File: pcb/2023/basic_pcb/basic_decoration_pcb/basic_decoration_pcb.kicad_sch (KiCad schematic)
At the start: 16 parts, among them J1 Conn_01x15_Socket, J2 Conn_01x15_Socket, J3 Screw_Terminal_01x03, Q1 2N2219

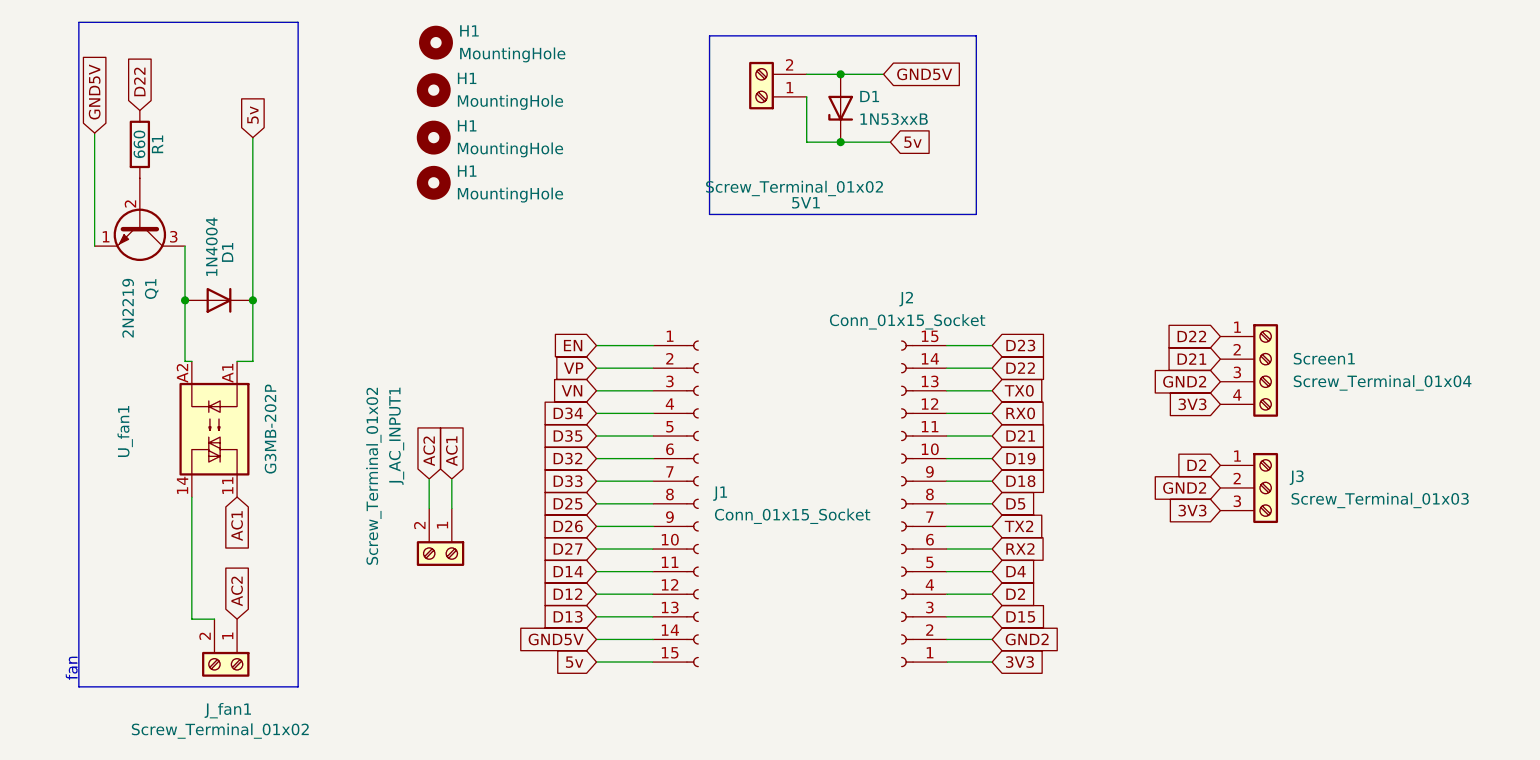
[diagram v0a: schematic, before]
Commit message: add, added custom solid state relay to the PCB by using optocouplers and triacs, also added the MOC3041 footprint to the esp32 library to keep it within our common resources
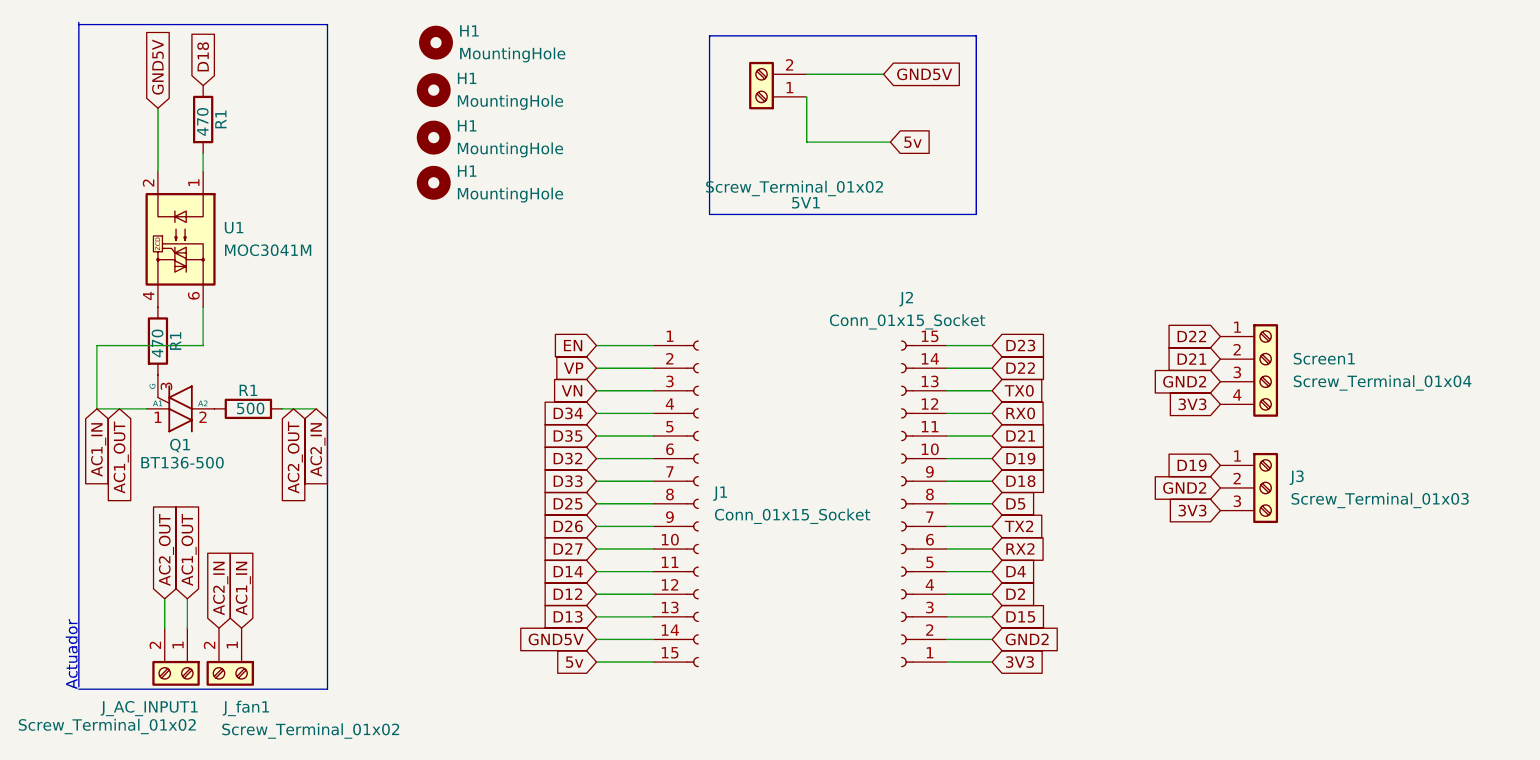
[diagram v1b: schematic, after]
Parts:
- removed D1: 1N53xxB, Diode_THT:D_DO-201_P15.24mm_Horizontal, symbol Diode:1N53xxB
- removed D1: 1N4004, Diode_THT:D_DO-41_SOD81_P10.16mm_Horizontal, symbol Diode:1N4004
- removed Q1: 2N2219, Package_TO_SOT_THT:TO-39-3, symbol Transistor_BJT:2N2219
- removed U_fan1: G3MB-202P, smart_sensor:G3MB-202P, symbol Relay_SolidState:34.81-8240
- added Q1: BT136-500, Package_TO_SOT_THT:TO-220-3_Vertical, symbol Triac_Thyristor:BT136-500
- added R1: 470, Resistor_THT:R_Axial_DIN0204_L3.6mm_D1.6mm_P5.08mm_Vertical, symbol Device:R
- added R1: 500, Resistor_THT:R_Axial_DIN0204_L3.6mm_D1.6mm_P5.08mm_Vertical, symbol Device:R
- added U1: MOC3041M, esp32:PDIP6_6P6X8P89_ONS, symbol Relay_SolidState:MOC3041M
- R1: value 660 -> 470
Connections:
- net D18: now also R1.1
- net D19: now also J3.1 (Pin_1)
- net D2: no longer J3.1 (Pin_1)
- net D22: no longer R1.1
- net GND5V: now also U1.2
- net AC2_IN: now reaches J_fan1.2 (Pin_2)
- net AC2_IN: now also J_AC_INPUT1.2 (Pin_2), R1.2
- net at R1.2: now also U1.1
- net AC1 renamed AC1_IN
- net AC1_IN: now also J_fan1.1 (Pin_1), Q1.1 (A1), U1.6
- removed net AC2: J_AC_INPUT1.2 (Pin_2), J_fan1.1 (Pin_1)
- new net: R1.1, U1.4
- new net: Q1.3 (G), R1.2
- new net: Q1.2 (A2), R1.1
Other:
- note added: "Actuador"
- note removed: "fan"
- moved on the sheet: J_fan1, R1

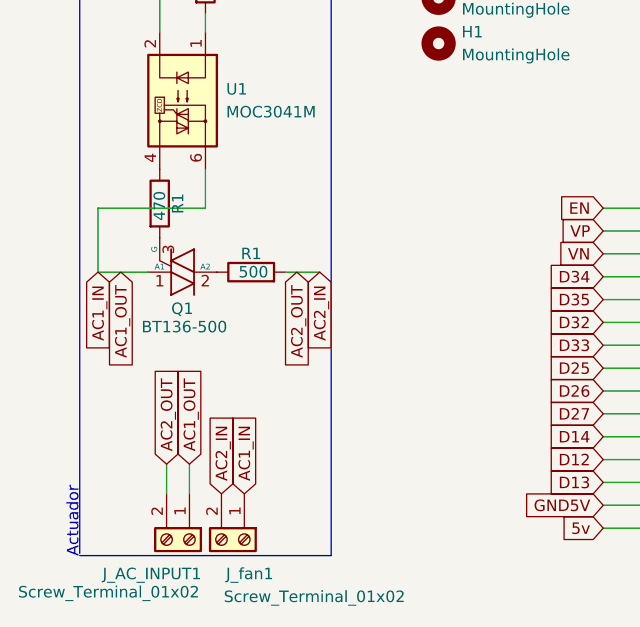
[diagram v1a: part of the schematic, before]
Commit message: update, fixed an error in the PCB and now any AC appliance which get's connected can work
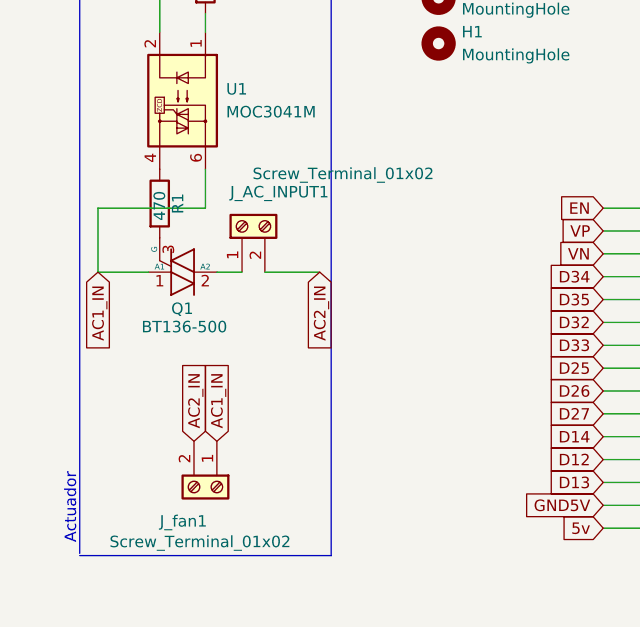
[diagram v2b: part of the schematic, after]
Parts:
- removed R1: 500, Resistor_THT:R_Axial_DIN0204_L3.6mm_D1.6mm_P5.08mm_Vertical, symbol Device:R
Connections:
- net AC1_IN: no longer J_AC_INPUT1.1 (Pin_1)
- net at Q1.2 (A2): now also J_AC_INPUT1.1 (Pin_1)
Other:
- moved on the sheet: J_fan1
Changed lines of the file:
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@@
-    (stroke (width 0) (type default))
-  )
-  (wire (pts (xy 33.528 93.98) (xy 33.528 90.678))
     (stroke (width 0) (type default))
   )
@@
     (stroke (width 0) (type default))
   )
-  (wire (pts (xy 46.736 69.342) (xy 50.546 69.342))
-    (stroke (width 0) (type default))
-  )
   (polyline (pts (xy 94.742 27.432) (xy 124.714 27.432))
     (stroke (width 0) (type default))
@@
     (stroke (width 0) (type default))
   )
+  (wire (pts (xy 39.116 69.342) (xy 41.91 69.342))
+    (stroke (width 0) (type default))
+  )
   (wire (pts (xy 105.664 39.37) (xy 115.062 39.37))
     (stroke (width 0) (type default))
@@
     (stroke (width 0) (type default))
   )
+  (wire (pts (xy 44.45 69.342) (xy 50.546 69.342))
+    (stroke (width 0) (type default))
+  )
   (wire (pts (xy 82.042 62.23) (xy 88.392 62.23))
     (stroke (width 0) (type default))
@@
     (stroke (width 0) (type default))
   )
-  (wire (pts (xy 36.068 93.98) (xy 36.068 90.678))
-    (stroke (width 0) (type default))
-  )
   (wire (pts (xy 82.042 97.79) (xy 88.392 97.79))
     (stroke (width 0) (type default))
   )
-  (text "Actuador\n" (at 23.876 93.218 90)
+  (text "Actuador\n" (at 23.622 91.694 90)
     (effects (font (size 1.27 1.27)) (justify right bottom))
   )
@@
     )
   )
-  (global_label "AC2_IN" (shape input) (at 39.624 93.98 90) (fields_autoplaced)
-    (effects (font (size 1.27 1.27)) (justify left))
-    (property "Intersheetrefs" "${INTERSHEET_REFS}" (at 39.624 84.5238 90)
+  (global_label "AC2_IN" (shape input) (at 36.576 88.138 90) (fields_autoplaced)
+    (effects (font (size 1.27 1.27)) (justify left))
+    (property "Intersheetrefs" "${INTERSHEET_REFS}" (at 36.576 78.6818 90)
       (effects (font (size 1.27 1.27)) (justify left) hide)
     )
@@
     )
   )
-  (global_label "AC1_IN" (shape input) (at 42.164 93.98 90) (fields_autoplaced)
-    (effects (font (size 1.27 1.27)) (justify left))
-    (property "Intersheetrefs" "${INTERSHEET_REFS}" (at 42.164 84.5238 90)
-      (effects (font (size 1.27 1.27)) (justify left) hide)
-    )
-  )
-  (global_label "AC2_OUT" (shape input) (at 48.006 69.342 270) (fields_autoplaced)
-    (effects (font (size 1.27 1.27)) (justify right))
-    (property "Intersheetrefs" "${INTERSHEET_REFS}" (at 48.006 80.4915 90)
-      (effects (font (size 1.27 1.27)) (justify right) hide)
+  (global_label "AC1_IN" (shape input) (at 39.116 88.138 90) (fields_autoplaced)
+    (effects (font (size 1.27 1.27)) (justify left))
+    (property "Intersheetrefs" "${INTERSHEET_REFS}" (at 39.116 78.6818 90)
+      (effects (font (size 1.27 1.27)) (justify left) hide)
     )
   )
@@
     )
   )
-  (global_label "AC2_OUT" (shape input) (at 33.528 90.678 90) (fields_autoplaced)
-    (effects (font (size 1.27 1.27)) (justify left))
-    (property "Intersheetrefs" "${INTERSHEET_REFS}" (at 33.528 79.5285 90)
-      (effects (font (size 1.27 1.27)) (justify left) hide)
-    )
-  )
   (global_label "GND5V" (shape input) (at 82.042 95.25 180) (fields_autoplaced)
     (effects (font (size 1.27 1.27)) (justify right))
@@
     )
   )
-  (global_label "AC1_OUT" (shape input) (at 28.448 69.342 270) (fields_autoplaced)
-    (effects (font (size 1.27 1.27)) (justify right))
-    (property "Intersheetrefs" "${INTERSHEET_REFS}" (at 28.448 80.4915 90)
-      (effects (font (size 1.27 1.27)) (justify right) hide)
-    )
-  )
   (global_label "VN" (shape input) (at 82.042 67.31 180) (fields_autoplaced)
     (effects (font (size 1.27 1.27)) (justify right))
@@
     (property "Intersheetrefs" "${INTERSHEET_REFS}" (at 144.0808 66.294 0)
       (effects (font (size 1.27 1.27)) (justify right) hide)
-    )
-  )
-  (global_label "AC1_OUT" (shape input) (at 36.068 90.678 90) (fields_autoplaced)
-    (effects (font (size 1.27 1.27)) (justify left))
-    (property "Intersheetrefs" "${INTERSHEET_REFS}" (at 36.068 79.5285 90)
-      (effects (font (size 1.27 1.27)) (justify left) hide)
     )
   )
@@
     )
   )
-  (symbol (lib_id "Connector:Screw_Terminal_01x02") (at 42.164 99.06 270) (unit 1)
-    (in_bom yes) (on_board yes) (dnp no)
-    (property "Reference" "J_fan1" (at 40.132 102.87 90)
-      (effects (font (size 1.27 1.27)) (justify left))
-    )
-    (property "Value" "Screw_Terminal_01x02" (at 39.878 105.41 90)
-      (effects (font (size 1.27 1.27)) (justify left))
-    )
-    (property "Footprint" "TerminalBlock:TerminalBlock_Altech_AK300-2_P5.00mm" (at 42.164 99.06 0)
-      (effects (font (size 1.27 1.27)) hide)
-    )
-    (property "Datasheet" "~" (at 42.164 99.06 0)
+  (symbol (lib_id "Connector:Screw_Terminal_01x02") (at 39.116 93.218 270) (unit 1)
+    (in_bom yes) (on_board yes) (dnp no)
+    (property "Reference" "J_fan1" (at 32.766 97.028 90)
+      (effects (font (size 1.27 1.27)) (justify left))
+    )
+    (property "Value" "Screw_Terminal_01x02" (at 27.178 99.314 90)
+      (effects (font (size 1.27 1.27)) (justify left))
+    )
+    (property "Footprint" "TerminalBlock:TerminalBlock_Altech_AK300-2_P5.00mm" (at 39.116 93.218 0)
+      (effects (font (size 1.27 1.27)) hide)
+    )
+    (property "Datasheet" "~" (at 39.116 93.218 0)
       (effects (font (size 1.27 1.27)) hide)
     )
@@
       (project "basic_decoration_pcb"
         (path "/e2e9caae-b3c7-4a5d-81db-191a274f7dfe"
-          (reference "J_AC_OUT1") (unit 1)
+          (reference "J_AC_INPUT1") (unit 1)
         )
       )
@@
     )
   )
-  (symbol (lib_id "Connector:Screw_Terminal_01x02") (at 36.068 99.06 270) (unit 1)
-    (in_bom yes) (on_board yes) (dnp no)
-    (property "Reference" "J_AC_INPUT1" (at 26.416 102.87 90)
-      (effects (font (size 1.27 1.27)) (justify left))
-    )
-    (property "Value" "Screw_Terminal_01x02" (at 17.018 104.902 90)
-      (effects (font (size 1.27 1.27)) (justify left))
-    )
-    (property "Footprint" "TerminalBlock:TerminalBlock_Altech_AK300-2_P5.00mm" (at 36.068 99.06 0)
-      (effects (font (size 1.27 1.27)) hide)
-    )
-    (property "Datasheet" "~" (at 36.068 99.06 0)
+  (symbol (lib_id "Triac_Thyristor:BT136-500") (at 35.306 69.342 270) (unit 1)
+    (in_bom yes) (on_board yes) (dnp no)
+    (property "Reference" "Q1" (at 34.036 73.406 90)
+      (effects (font (size 1.27 1.27)) (justify left))
+    )
+    (property "Value" "BT136-500" (at 30.734 75.438 90)
+      (effects (font (size 1.27 1.27)) (justify left))
+    )
+    (property "Footprint" "Package_TO_SOT_THT:TO-220-3_Vertical" (at 33.401 74.422 0)
+      (effects (font (size 1.27 1.27) italic) (justify left) hide)
+    )
+    (property "Datasheet" "http://www.micropik.com/PDF/BT136-600.pdf" (at 35.306 69.342 0)
+      (effects (font (size 1.27 1.27)) (justify left) hide)
+    )
+    (pin "1")
+    (pin "2")
+    (pin "3")
+    (instances
+      (project "basic_decoration_pcb"
+        (path "/e2e9caae-b3c7-4a5d-81db-191a274f7dfe"
+          (reference "Q1") (unit 1)
+        )
+      )
+    )
+  )
+  (symbol (lib_id "Connector:Screw_Terminal_01x02") (at 41.91 64.262 90) (unit 1)
+    (in_bom yes) (on_board yes) (dnp no)
+    (property "Reference" "J_AC_INPUT1" (at 51.562 60.452 90)
+      (effects (font (size 1.27 1.27)) (justify left))
+    )
+    (property "Value" "Screw_Terminal_01x02" (at 63.246 58.42 90)
+      (effects (font (size 1.27 1.27)) (justify left))
+    )
+    (property "Footprint" "TerminalBlock:TerminalBlock_Altech_AK300-2_P5.00mm" (at 41.91 64.262 0)
+      (effects (font (size 1.27 1.27)) hide)
+    )
+    (property "Datasheet" "~" (at 41.91 64.262 0)
       (effects (font (size 1.27 1.27)) hide)
     )
@@
       (project "basic_decoration_pcb"
         (path "/e2e9caae-b3c7-4a5d-81db-191a274f7dfe"
-          (reference "J_AC_INPUT1") (unit 1)
+          (reference "J_AC_LOAD1") (unit 1)
         )
       )
@@
         )
       )
-    )
-  )
-  (symbol (lib_id "Triac_Thyristor:BT136-500") (at 35.306 69.342 270) (unit 1)
-    (in_bom yes) (on_board yes) (dnp no)
-    (property "Reference" "Q1" (at 34.036 73.406 90)
-      (effects (font (size 1.27 1.27)) (justify left))
-    )
-    (property "Value" "BT136-500" (at 30.734 75.438 90)
-      (effects (font (size 1.27 1.27)) (justify left))
-    )
-    (property "Footprint" "Package_TO_SOT_THT:TO-220-3_Vertical" (at 33.401 74.422 0)
-      (effects (font (size 1.27 1.27) italic) (justify left) hide)
-    )
-    (property "Datasheet" "http://www.micropik.com/PDF/BT136-600.pdf" (at 35.306 69.342 0)
-      (effects (font (size 1.27 1.27)) (justify left) hide)
-    )
-    (pin "1")
-    (pin "2")
-    (pin "3")
-    (instances
-      (project "basic_decoration_pcb"
-        (path "/e2e9caae-b3c7-4a5d-81db-191a274f7dfe"
-          (reference "Q1") (unit 1)
-        )
-      )
-    )
-  )
-  (symbol (lib_id "Device:R") (at 42.926 69.342 90) (unit 1)
-    (in_bom yes) (on_board yes) (dnp no)
-    (property "Reference" "R1" (at 42.926 67.31 90)
-      (effects (font (size 1.27 1.27)))
-    )
-    (property "Value" "500" (at 43.18 69.342 90)
-      (effects (font (size 1.27 1.27)))
-    )
-    (property "Footprint" "Resistor_THT:R_Axial_DIN0204_L3.6mm_D1.6mm_P5.08mm_Vertical" (at 42.926 71.12 90)
-      (effects (font (size 1.27 1.27)) hide)
-    )
-    (property "Datasheet" "~" (at 42.926 69.342 0)
-      (effects (font (size 1.27 1.27)) hide)
-    )
-    (pin "1")
-    (pin "2")
-    (instances
-      (project "power_control"
-        (path "/4e3cb747-cdef-484c-aee7-ba21bcfd1bd4"
-          (reference "R1") (unit 1)
-        )
-      )
-      (project "basic_decoration_pcb"
-        (path "/e2e9caae-b3c7-4a5d-81db-191a274f7dfe"
-          (reference "R3") (unit 1)
-        )
-      )
-      (project "intregration1"
-        (path "/eb698b21-5dce-4ccc-89a9-0cb444bd0145"
-          (reference "R2") (unit 1)
-        )
-      )

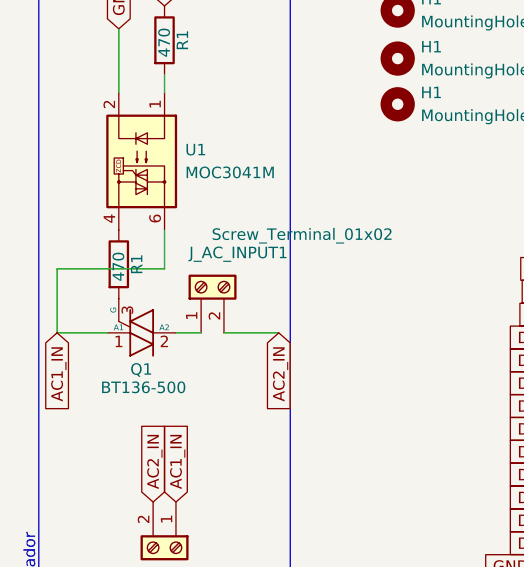
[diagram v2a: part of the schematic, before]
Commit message: update, fixed bug on the PCB, a wrong connection between the BT136 and the actuators wasn't making it work
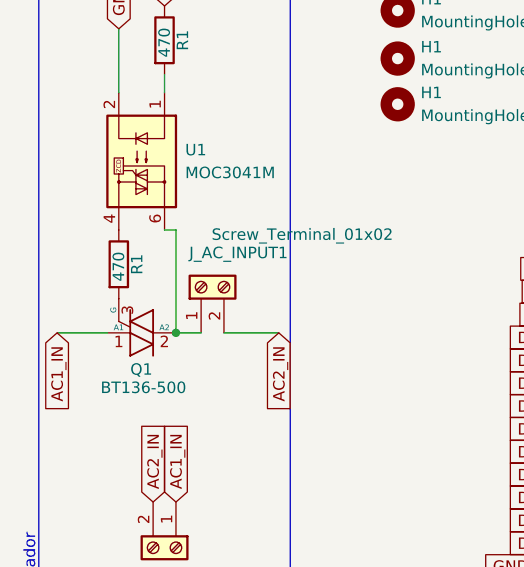
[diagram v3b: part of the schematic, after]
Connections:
- net AC1_IN: no longer U1.6
- net at J_AC_INPUT1.1 (Pin_1), Q1.2 (A2): now also U1.6
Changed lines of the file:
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@@
 (kicad_sch (version 20230121) (generator eeschema)
   (paper "A4")
+  (junction (at 39.116 69.342) (diameter 0) (color 0 0 0 0)
+  )
   (wire (pts (xy 121.412 64.77) (xy 126.492 64.77))
     (stroke (width 0) (type default))
@@
   )
   (polyline (pts (xy 51.816 100.838) (xy 51.816 26.162))
-    (stroke (width 0) (type default))
-  )
-  (wire (pts (xy 37.846 62.23) (xy 25.908 62.23))
     (stroke (width 0) (type default))
   )
@@
     (stroke (width 0) (type default))
   )
-  (wire (pts (xy 37.846 57.912) (xy 37.846 62.23))
-    (stroke (width 0) (type default))
-  )
   (polyline (pts (xy 94.742 27.432) (xy 124.714 27.432))
     (stroke (width 0) (type default))
@@
   )
   (wire (pts (xy 121.412 85.09) (xy 126.492 85.09))
-    (stroke (width 0) (type default))
-  )
-  (wire (pts (xy 39.116 69.342) (xy 41.91 69.342))
     (stroke (width 0) (type default))
   )
@@
     (stroke (width 0) (type default))
   )
-  (wire (pts (xy 25.908 62.23) (xy 25.908 69.342))
+  (wire (pts (xy 82.042 90.17) (xy 88.392 90.17))
     (stroke (width 0) (type default))
   )
-  (wire (pts (xy 82.042 90.17) (xy 88.392 90.17))
+  (wire (pts (xy 39.116 69.342) (xy 41.91 69.342))
     (stroke (width 0) (type default))
   )
@@
   )
   (wire (pts (xy 82.042 62.23) (xy 88.392 62.23))
+    (stroke (width 0) (type default))
+  )
+  (wire (pts (xy 39.116 57.912) (xy 39.116 69.342))
     (stroke (width 0) (type default))
   )
@@
     (stroke (width 0) (type default))
   )
+  (wire (pts (xy 37.846 57.912) (xy 39.116 57.912))
+    (stroke (width 0) (type default))
+  )
